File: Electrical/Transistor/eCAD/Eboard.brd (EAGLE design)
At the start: 160 x 100 mm, 22 parts

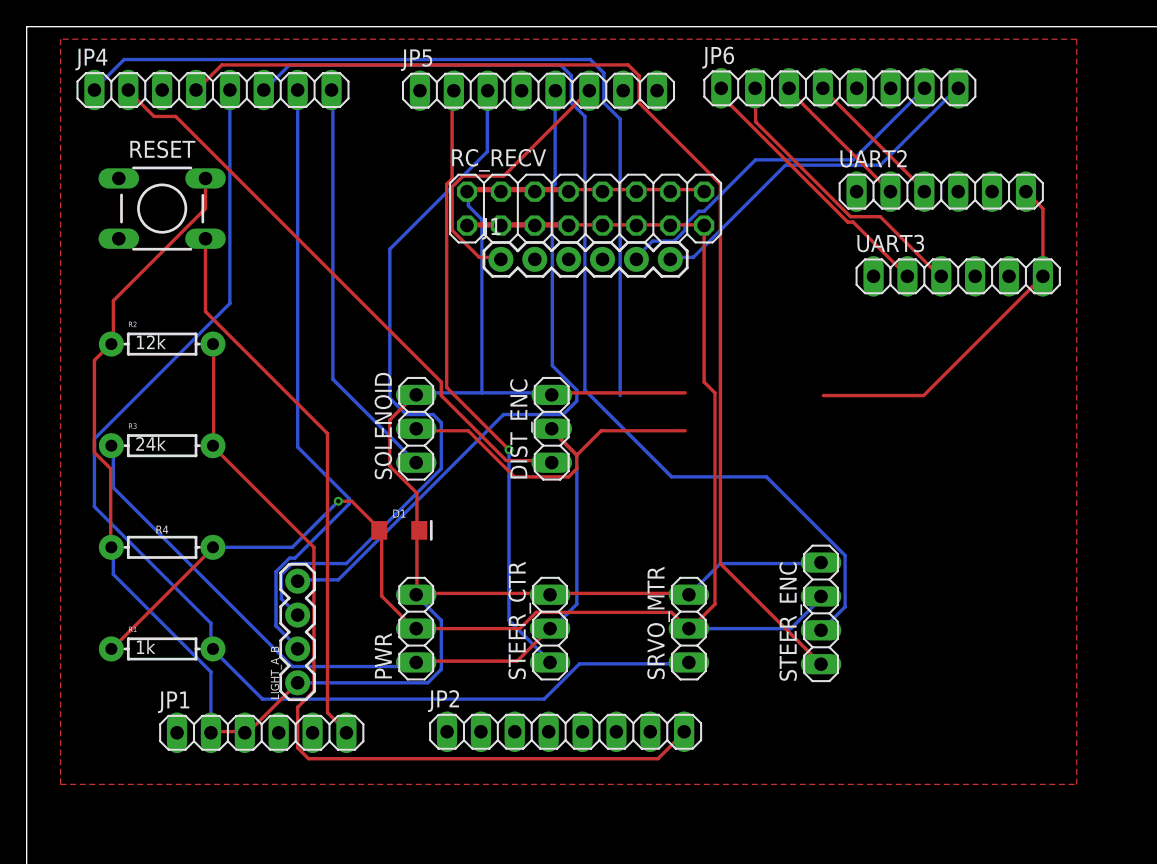
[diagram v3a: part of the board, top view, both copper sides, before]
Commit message: performed autorouter and drc, about to change 5v to 16mils and 12v to 40mils.
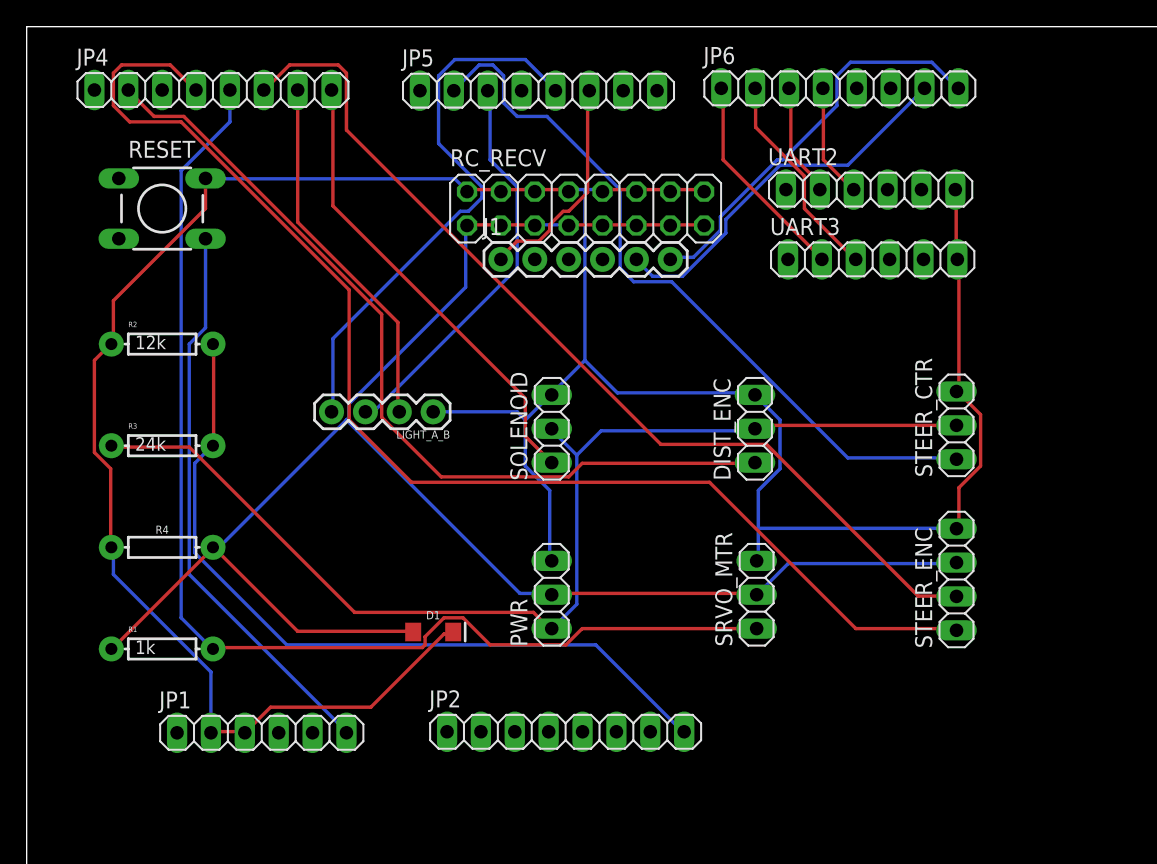
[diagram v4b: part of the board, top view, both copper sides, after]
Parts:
- moved STEER_CTR 34.1 mm to (69.7, 70.1)
- moved LIGHT_A_B 22.7 mm to (30.5, 71.1), turned to 180 degrees
- moved DIST_ENC 15.2 mm to (54.6, 69.8)
- moved PWR 10.5 mm to (39.4, 57.4)
- moved STEER_ENC 10.5 mm to (69.7, 58.5)
- moved SOLENOID 10.2 mm to (39.4, 69.8)
- moved D1 8.03 mm to (30.5, 54.6)
- moved UART3 6.54 mm to (63.4, 82.5)
- moved SRVO_MTR 5.68 mm to (54.7, 57.4)
- moved UART2 5.30 mm to (63.3, 87.8)
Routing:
- net 12V_BKUP: track 64.3 -> 0.00 mm
- net LIGHT_A2: track 53.0 -> 30.1 mm
- net DIST_ENC: track 43.9 -> 64.0 mm
- net LIGHT_B: track 46.7 -> 27.3 mm
- net 5V: track 116.4 -> 131.1 mm, vias 1 -> 0
- net GND: track 205.1 -> 217.3 mm
- net STEER_ENC1: track 84.1 -> 94.9 mm
- net STEER_CTR: track 46.3 -> 55.4 mm, vias 1 -> 0
- net LIGHT_A1: track 50.7 -> 41.9 mm
- net STEER_ENC2: track 79.2 -> 71.7 mm
- net VBATT_ADC: track 64.1 -> 58.6 mm
- net UART3_RX: track 21.2 -> 16.0 mm
- net J1_1: track 21.2 -> 16.6 mm
- net SOLENOID: track 30.6 -> 34.8 mm
- net UART3_TX: track 20.1 -> 16.0 mm
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- removed copper zone on layer 1, net N$1
